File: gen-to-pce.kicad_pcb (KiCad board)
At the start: 2 copper layers, 69.8 x 24.1 mm, 5 parts, among them J1 DB9_Male, J2 Conn_01x08_Female, U1 74HC04, U2 74HC74, U3 74HC157

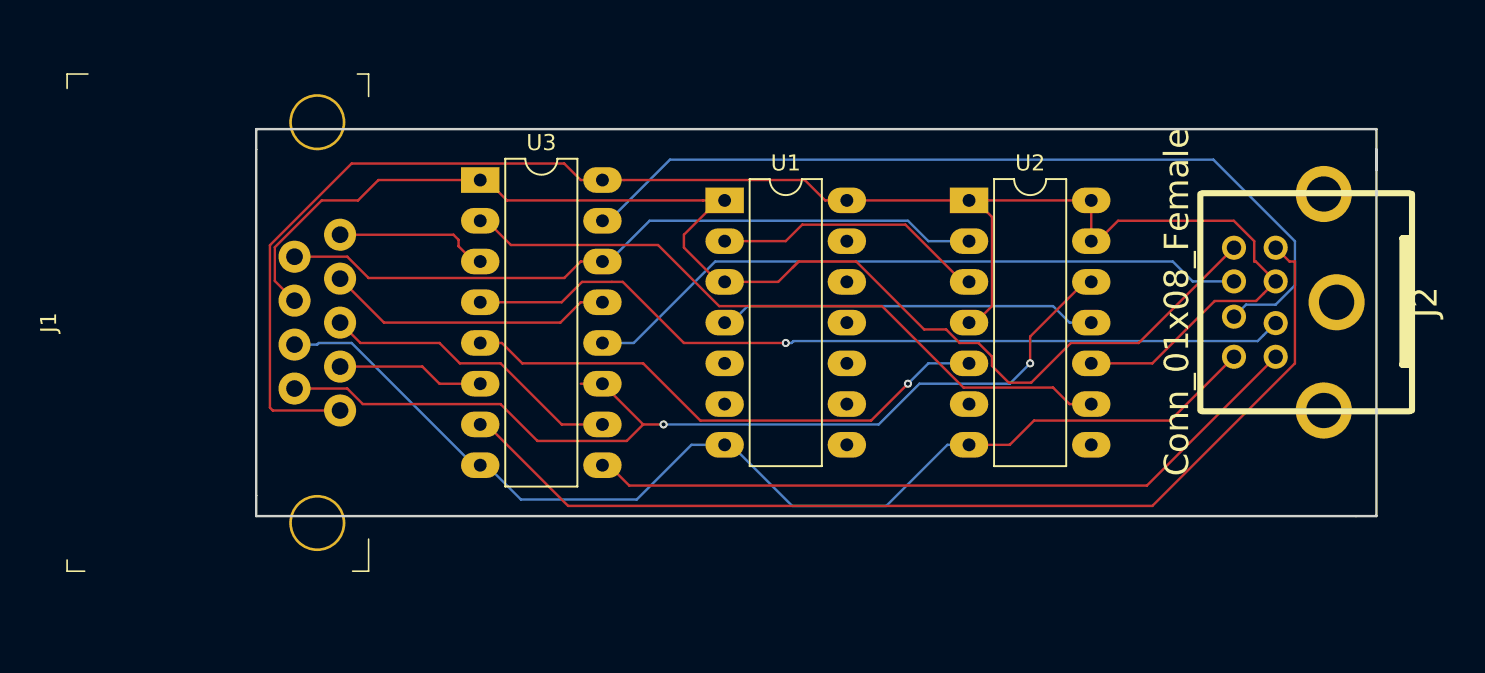
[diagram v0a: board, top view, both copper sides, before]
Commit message: More silkscreen labels, better traces
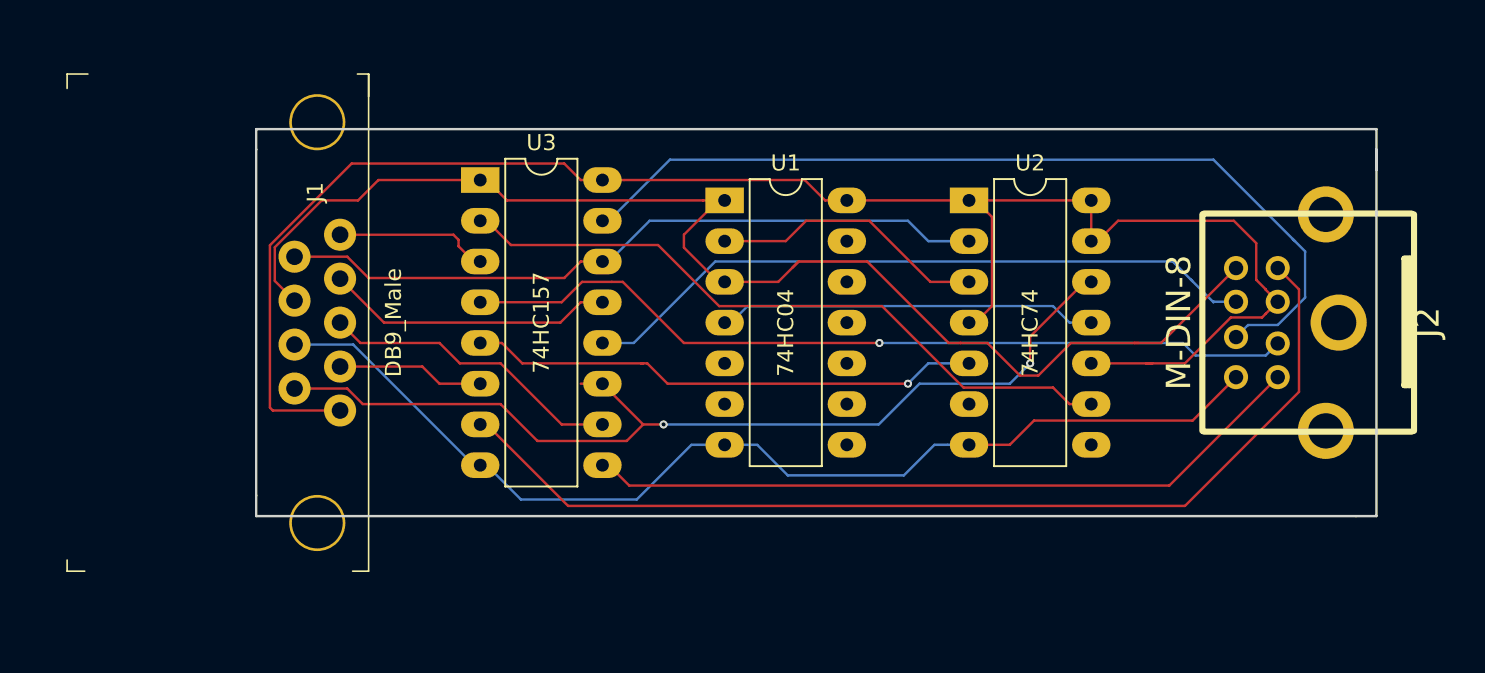
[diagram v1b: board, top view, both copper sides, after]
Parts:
- J2: value Conn_01x08_Female -> M-DIN-8
- moved J2 1.28 mm to (162.7, 87.6)
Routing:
- net Net-(J2-Pad7): track 54.2 -> 56.2 mm
- net Net-(U2-Pad5): track 34.0 -> 32.2 mm
- net GND: track 69.5 -> 67.8 mm
- net +5V: track 108.6 -> 109.9 mm
- net Net-(J2-Pad4): track 42.4 -> 43.2 mm
- net Net-(J1-Pad7): track 82.4 -> 81.7 mm
- net Net-(U1-Pad2): track 17.1 -> 17.7 mm
- net Net-(J2-Pad2): track 52.2 -> 52.6 mm, vias 2 -> 1

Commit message: Ground fill, larger power traces, rectanglular edge cuts
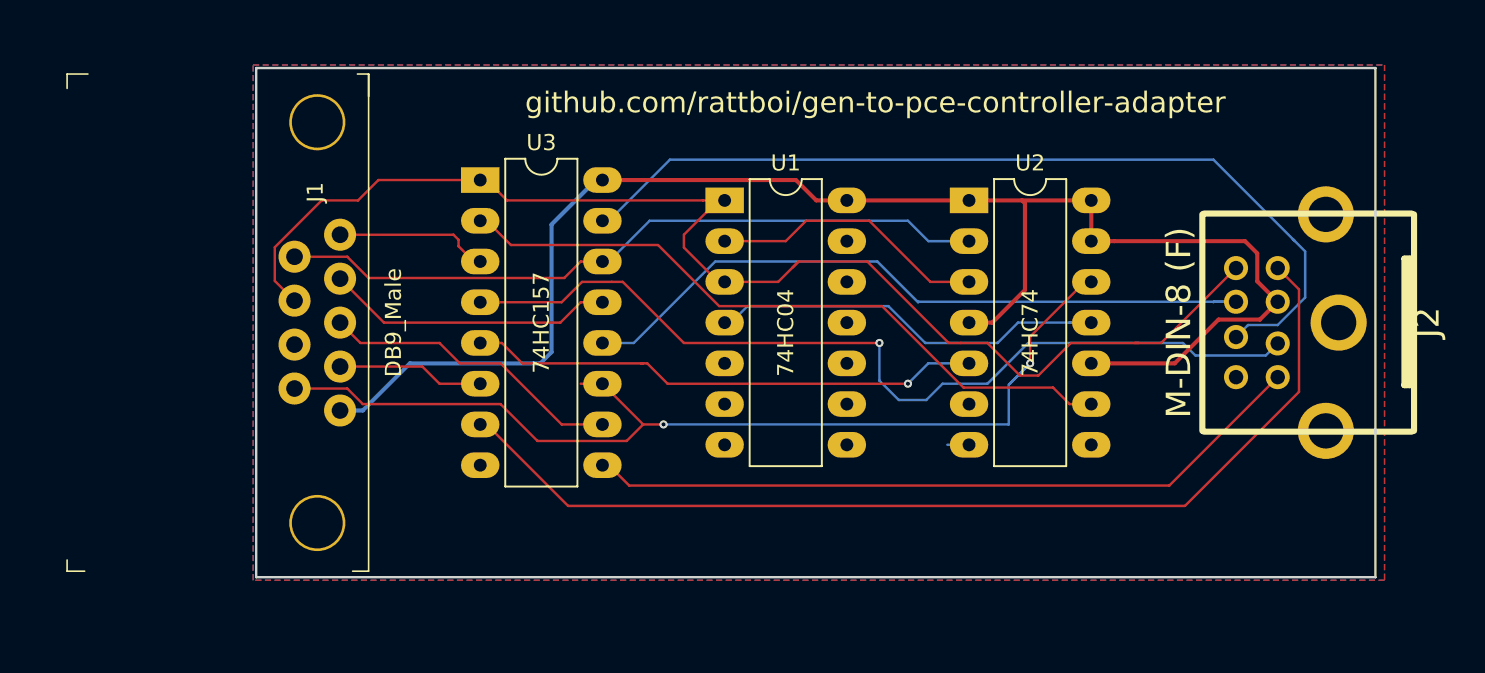
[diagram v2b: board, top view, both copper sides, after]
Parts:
- J2: value M-DIN-8 -> M-DIN-8 (F)
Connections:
- U1 pad 10: (no net) -> Net-(U1-Pad10)
- U1 pad 11: (no net) -> GND
- U1 pad 12: (no net) -> Net-(U1-Pad12)
- U1 pad 13: (no net) -> GND
- U1 pad 5: (no net) -> GND
- U1 pad 6: (no net) -> Net-(U1-Pad6)
- U1 pad 8: (no net) -> Net-(U1-Pad8)
- U1 pad 9: (no net) -> GND
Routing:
- net GND: track 67.8 -> 2.55 mm
- net +5V: track 109.9 -> 102.2 mm
- net Net-(J2-Pad2): track 52.6 -> 56.9 mm
- net Net-(J1-Pad9): track 61.1 -> 64.3 mm
- net Net-(U1-Pad4): track 23.7 -> 26.1 mm
- net Net-(J2-Pad4): track 43.2 -> 44.5 mm
- added copper zone on B.Cu, net GND
- added copper zone on F.Cu, net GND
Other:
- board size 69.8 x 24.1 mm -> 69.8 x 31.8 mm
- board text added: "github.com/rattboi/gen-to-pce-controller-adapter"

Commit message: M-din-8 mount holes plated, select line delay
Added select line delay for genesis controller to make sure there's no
problem with propagation delay and setup time.
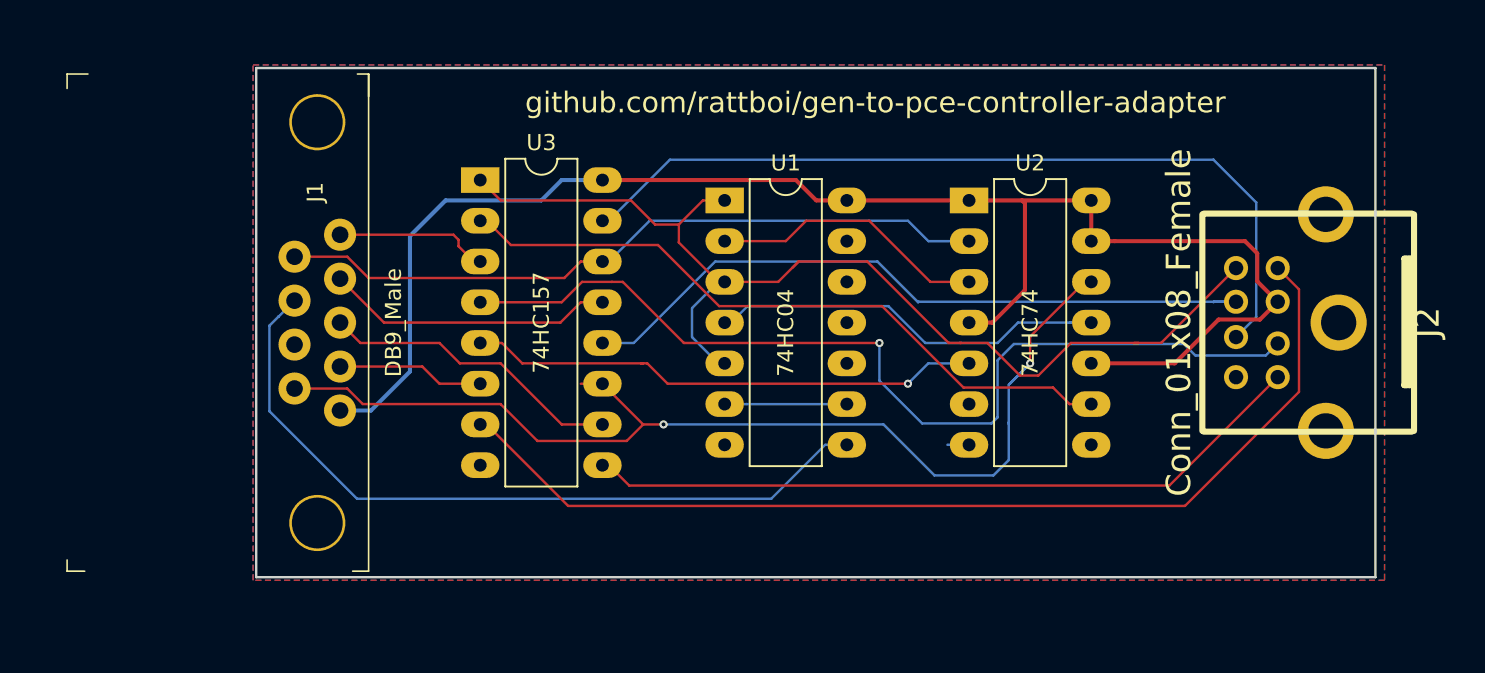
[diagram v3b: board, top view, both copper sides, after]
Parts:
- J2: value M-DIN-8 (F) -> Conn_01x08_Female
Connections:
- J2 pad 6: Net-(J1-Pad7) -> Net-(J2-Pad6)
- U1 pad 1: Net-(J1-Pad7) -> Net-(J2-Pad6)
- U1 pad 3: Net-(J1-Pad7) -> Net-(J2-Pad6)
- U1 pad 5: GND -> Net-(J2-Pad6)
- U1 pad 8: Net-(U1-Pad8) -> Net-(J1-Pad7)
- U1 pad 9: GND -> Net-(U1-Pad6)
- U3 pad 1: Net-(J1-Pad7) -> Net-(J2-Pad6)
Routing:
- net Net-(J2-Pad6): track 0.00 -> 69.9 mm
- net Net-(J1-Pad7): track 81.7 -> 47.2 mm
- net Net-(U1-Pad6): track 0.00 -> 7.62 mm
- net Net-(J1-Pad9): track 64.3 -> 68.4 mm
- net Net-(J2-Pad7): track 56.2 -> 52.4 mm
- net Net-(J2-Pad2): track 56.9 -> 60.2 mm
- net +5V: track 102.2 -> 102.9 mm

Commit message: Fixed up silkscreen, added oshw + kicad logos
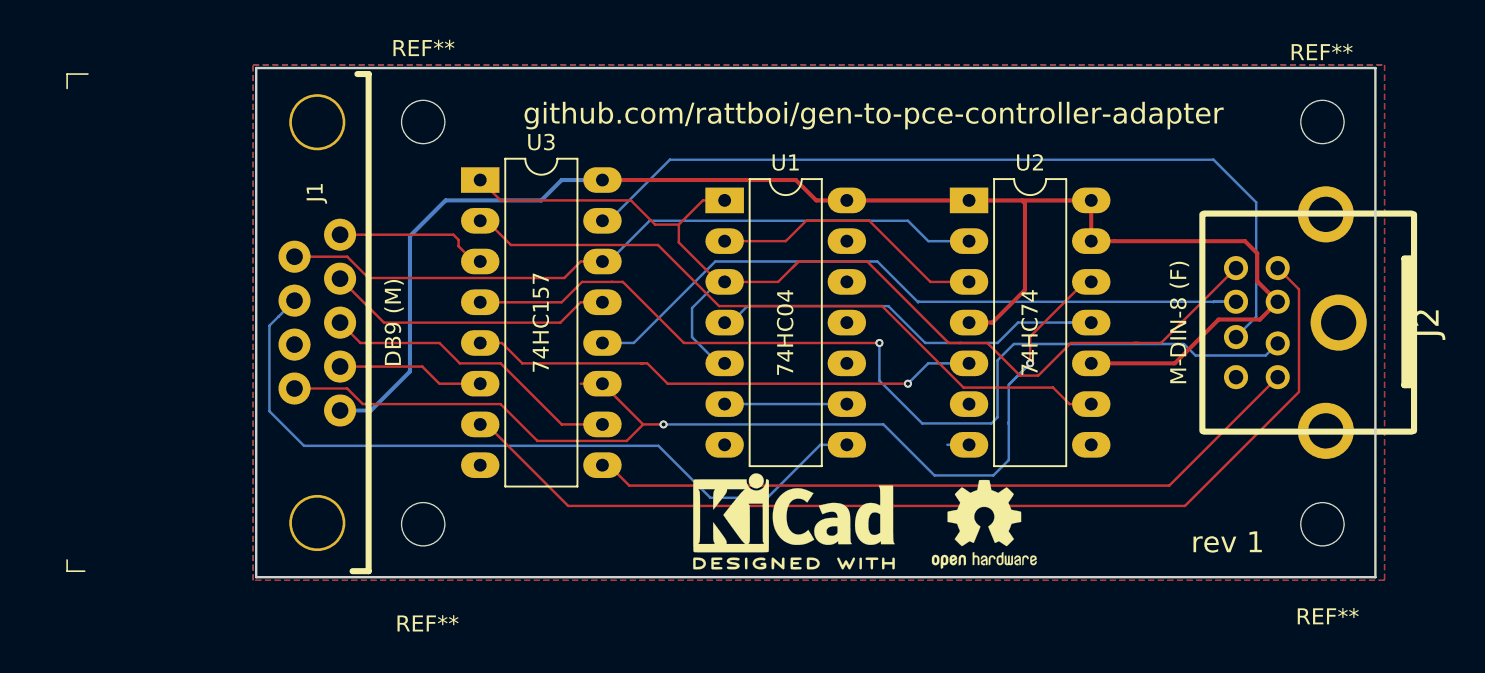
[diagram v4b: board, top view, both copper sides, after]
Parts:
- added REF**: MountingHole_2.7mm_M2.5, MountingHole:MountingHole_2.7mm_M2.5, F.Cu at (108.2, 100.3)
- added REF**: MountingHole_2.7mm_M2.5, MountingHole:MountingHole_2.7mm_M2.5, F.Cu at (108.3, 74.8)
- added REF**: MountingHole_2.7mm_M2.5, MountingHole:MountingHole_2.7mm_M2.5, F.Cu at (164.2, 75.1)
- added REF**: MountingHole_2.7mm_M2.5, MountingHole:MountingHole_2.7mm_M2.5, F.Cu at (164.3, 100.2)
- added REF**: OSHW-Logo2_7.3x6mm_SilkScreen, Symbol:OSHW-Logo2_7.3x6mm_SilkScreen, F.Cu at (143.2, 100.2)
- added REF**: KiCad-Logo2_6mm_SilkScreen, Symbol:KiCad-Logo2_6mm_SilkScreen, F.Cu at (131.3, 100.0)
- J1: value DB9_Male -> DB9 (M)
- J2: value Conn_01x08_Female -> M-DIN-8 (F)
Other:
- board text added: "rev 1"
